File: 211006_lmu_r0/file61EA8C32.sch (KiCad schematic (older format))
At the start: 15 parts

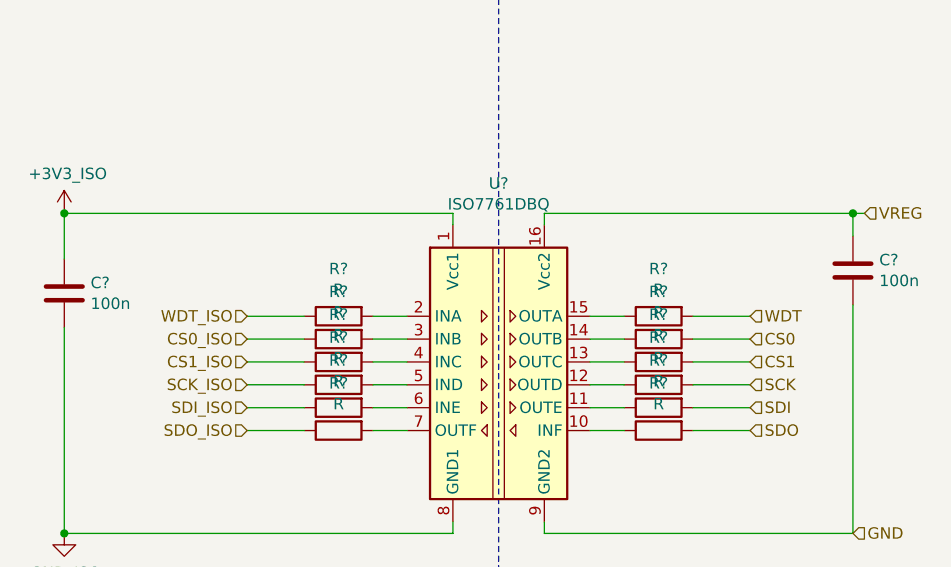
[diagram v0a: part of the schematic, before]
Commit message: Updated BOM and footprints for non-hv components
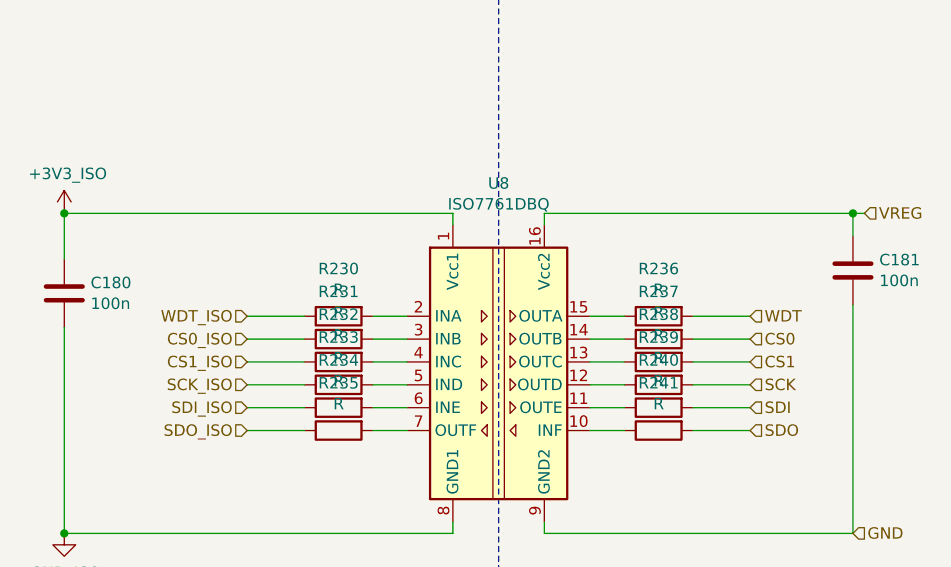
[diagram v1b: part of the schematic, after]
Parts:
- gave numbers to parts that had none: 15
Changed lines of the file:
@@
 SCK_ISO
 $Comp
-L +3v3_iso:+3V3_ISO #PWR?
+L +3v3_iso:+3V3_ISO #PWR0171
 U 1 1 62444AD5
 P 3800 2950
-AR Path="/61EA8C33/62444AD5" Ref="#PWR?"  Part="1"
+AR Path="/61EA8C33/62444AD5" Ref="#PWR0171"  Part="1"
 AR Path="/624497CF/62444AD5" Ref="#PWR?"  Part="1"
 AR Path="/62454BCB/62444AD5" Ref="#PWR?"  Part="1"
-AR Path="/6248C6B3/62444AD5" Ref="#PWR?"  Part="1"
-AR Path="/6248F546/62444AD5" Ref="#PWR?"  Part="1"
-F 0 "#PWR?" H 3800 2800 50  0001 C CNN
+AR Path="/6248C6B3/62444AD5" Ref="#PWR0173"  Part="1"
+AR Path="/6248F546/62444AD5" Ref="#PWR0175"  Part="1"
+F 0 "#PWR0175" H 3800 2800 50  0001 C CNN
 F 1 "+3V3_ISO" H 3815 3123 50  0000 C CNN
 F 2 "" H 3800 2950 50  0001 C CNN
@@
 P 5700 3700
 AR Path="/62454BCB/62479198" Ref="U?"  Part="1"
-AR Path="/61EA8C33/62479198" Ref="U?"  Part="1"
-AR Path="/6248C6B3/62479198" Ref="U?"  Part="1"
-AR Path="/6248F546/62479198" Ref="U?"  Part="1"
-F 0 "U?" H 5700 4581 50  0000 C CNN
+AR Path="/61EA8C33/62479198" Ref="U6"  Part="1"
+AR Path="/6248C6B3/62479198" Ref="U7"  Part="1"
+AR Path="/6248F546/62479198" Ref="U8"  Part="1"
+F 0 "U8" H 5700 4581 50  0000 C CNN
 F 1 "ISO7761DBQ" H 5700 4490 50  0000 C CNN
 F 2 "Package_SO:SSOP-16_3.9x4.9mm_P0.635mm" H 5925 3150 50  0001 L CNN
@@
 P 7250 3200
 AR Path="/62454BCB/6247B7F3" Ref="C?"  Part="1"
-AR Path="/61EA8C33/6247B7F3" Ref="C?"  Part="1"
-AR Path="/6248C6B3/6247B7F3" Ref="C?"  Part="1"
-AR Path="/6248F546/6247B7F3" Ref="C?"  Part="1"
-F 0 "C?" H 7365 3246 50  0000 L CNN
+AR Path="/61EA8C33/6247B7F3" Ref="C177"  Part="1"
+AR Path="/6248C6B3/6247B7F3" Ref="C179"  Part="1"
+AR Path="/6248F546/6247B7F3" Ref="C181"  Part="1"
+F 0 "C181" H 7365 3246 50  0000 L CNN
 F 1 "100n" H 7365 3155 50  0000 L CNN
 F 2 "" H 7288 3050 50  0001 C CNN
@@
 P 3800 3300
 AR Path="/62454BCB/6247C6BA" Ref="C?"  Part="1"
-AR Path="/61EA8C33/6247C6BA" Ref="C?"  Part="1"
-AR Path="/6248C6B3/6247C6BA" Ref="C?"  Part="1"
-AR Path="/6248F546/6247C6BA" Ref="C?"  Part="1"
-F 0 "C?" H 3915 3346 50  0000 L CNN
+AR Path="/61EA8C33/6247C6BA" Ref="C176"  Part="1"
+AR Path="/6248C6B3/6247C6BA" Ref="C178"  Part="1"
+AR Path="/6248F546/6247C6BA" Ref="C180"  Part="1"
+F 0 "C180" H 3915 3346 50  0000 L CNN
 F 1 "100n" H 3915 3255 50  0000 L CNN
 F 2 "" H 3838 3150 50  0001 C CNN
@@
 $EndComp
 $Comp
-L gnd_iso:GND_ISO #PWR?
+L gnd_iso:GND_ISO #PWR0172
 U 1 1 62445214
 P 3800 4350
-AR Path="/61EA8C33/62445214" Ref="#PWR?"  Part="1"
+AR Path="/61EA8C33/62445214" Ref="#PWR0172"  Part="1"
 AR Path="/624497CF/62445214" Ref="#PWR?"  Part="1"
 AR Path="/62454BCB/62445214" Ref="#PWR?"  Part="1"
-AR Path="/6248C6B3/62445214" Ref="#PWR?"  Part="1"
-AR Path="/6248F546/62445214" Ref="#PWR?"  Part="1"
-F 0 "#PWR?" H 3800 4100 50  0001 C CNN
+AR Path="/6248C6B3/62445214" Ref="#PWR0174"  Part="1"
+AR Path="/6248F546/62445214" Ref="#PWR0176"  Part="1"
+F 0 "#PWR0176" H 3800 4100 50  0001 C CNN
 F 1 "GND_ISO" H 3805 4177 50  0000 C CNN
 F 2 "" H 3800 4350 50  0001 C CNN
@@
 	5500 2950 5500 3000
 $Comp
-L Device:R R?
+L Device:R R206
 U 1 1 626BF8F2
 P 5000 3400
-F 0 "R?" V 4793 3400 50  0000 C CNN
+AR Path="/61EA8C33/626BF8F2" Ref="R206"  Part="1"
+AR Path="/6248C6B3/626BF8F2" Ref="R218"  Part="1"
+AR Path="/6248F546/626BF8F2" Ref="R230"  Part="1"
+F 0 "R230" V 4793 3400 50  0000 C CNN
 F 1 "R" V 4884 3400 50  0000 C CNN
 F 2 "" V 4930 3400 50  0001 C CNN
@@
 $EndComp
 $Comp
-L Device:R R?
+L Device:R R207
 U 1 1 626C0FC4
 P 5000 3500
-F 0 "R?" V 4793 3500 50  0000 C CNN
+AR Path="/61EA8C33/626C0FC4" Ref="R207"  Part="1"
+AR Path="/6248C6B3/626C0FC4" Ref="R219"  Part="1"
+AR Path="/6248F546/626C0FC4" Ref="R231"  Part="1"
+F 0 "R231" V 4793 3500 50  0000 C CNN
 F 1 "R" V 4884 3500 50  0000 C CNN
 F 2 "" V 4930 3500 50  0001 C CNN
@@
 $EndComp
 $Comp
-L Device:R R?
+L Device:R R208
 U 1 1 626C1186
 P 5000 3600
-F 0 "R?" V 4793 3600 50  0000 C CNN
+AR Path="/61EA8C33/626C1186" Ref="R208"  Part="1"
+AR Path="/6248C6B3/626C1186" Ref="R220"  Part="1"
+AR Path="/6248F546/626C1186" Ref="R232"  Part="1"
+F 0 "R232" V 4793 3600 50  0000 C CNN
 F 1 "R" V 4884 3600 50  0000 C CNN
 F 2 "" V 4930 3600 50  0001 C CNN
@@
 $EndComp
 $Comp
-L Device:R R?
+L Device:R R209
 U 1 1 626C1339
 P 5000 3700
-F 0 "R?" V 4793 3700 50  0000 C CNN
+AR Path="/61EA8C33/626C1339" Ref="R209"  Part="1"
+AR Path="/6248C6B3/626C1339" Ref="R221"  Part="1"
+AR Path="/6248F546/626C1339" Ref="R233"  Part="1"
+F 0 "R233" V 4793 3700 50  0000 C CNN
 F 1 "R" V 4884 3700 50  0000 C CNN
 F 2 "" V 4930 3700 50  0001 C CNN
@@
 $EndComp
 $Comp
-L Device:R R?
+L Device:R R210
 U 1 1 626C148E
 P 5000 3800
-F 0 "R?" V 4793 3800 50  0000 C CNN
+AR Path="/61EA8C33/626C148E" Ref="R210"  Part="1"
+AR Path="/6248C6B3/626C148E" Ref="R222"  Part="1"
+AR Path="/6248F546/626C148E" Ref="R234"  Part="1"
+F 0 "R234" V 4793 3800 50  0000 C CNN
 F 1 "R" V 4884 3800 50  0000 C CNN
 F 2 "" V 4930 3800 50  0001 C CNN
@@
 $EndComp
 $Comp
-L Device:R R?
+L Device:R R211
 U 1 1 626C1651
 P 5000 3900
-F 0 "R?" V 4793 3900 50  0000 C CNN
+AR Path="/61EA8C33/626C1651" Ref="R211"  Part="1"
+AR Path="/6248C6B3/626C1651" Ref="R223"  Part="1"
+AR Path="/6248F546/626C1651" Ref="R235"  Part="1"
+F 0 "R235" V 4793 3900 50  0000 C CNN
 F 1 "R" V 4884 3900 50  0000 C CNN
 F 2 "" V 4930 3900 50  0001 C CNN
@@
 $EndComp
 $Comp
-L Device:R R?
+L Device:R R212
 U 1 1 626C3188
 P 6400 3400
-F 0 "R?" V 6193 3400 50  0000 C CNN
+AR Path="/61EA8C33/626C3188" Ref="R212"  Part="1"
+AR Path="/6248C6B3/626C3188" Ref="R224"  Part="1"
+AR Path="/6248F546/626C3188" Ref="R236"  Part="1"
+F 0 "R236" V 6193 3400 50  0000 C CNN
 F 1 "R" V 6284 3400 50  0000 C CNN
 F 2 "" V 6330 3400 50  0001 C CNN
@@
 $EndComp
 $Comp
-L Device:R R?
+L Device:R R213
 U 1 1 626C318E
 P 6400 3500
-F 0 "R?" V 6193 3500 50  0000 C CNN
+AR Path="/61EA8C33/626C318E" Ref="R213"  Part="1"
+AR Path="/6248C6B3/626C318E" Ref="R225"  Part="1"
+AR Path="/6248F546/626C318E" Ref="R237"  Part="1"
+F 0 "R237" V 6193 3500 50  0000 C CNN
 F 1 "R" V 6284 3500 50  0000 C CNN
 F 2 "" V 6330 3500 50  0001 C CNN
@@
 $EndComp
 $Comp
-L Device:R R?
+L Device:R R214
 U 1 1 626C3194
 P 6400 3600
-F 0 "R?" V 6193 3600 50  0000 C CNN
+AR Path="/61EA8C33/626C3194" Ref="R214"  Part="1"
+AR Path="/6248C6B3/626C3194" Ref="R226"  Part="1"
+AR Path="/6248F546/626C3194" Ref="R238"  Part="1"
+F 0 "R238" V 6193 3600 50  0000 C CNN
 F 1 "R" V 6284 3600 50  0000 C CNN
 F 2 "" V 6330 3600 50  0001 C CNN
@@
 $EndComp
 $Comp
-L Device:R R?
+L Device:R R215
 U 1 1 626C319A
 P 6400 3700
-F 0 "R?" V 6193 3700 50  0000 C CNN
+AR Path="/61EA8C33/626C319A" Ref="R215"  Part="1"
+AR Path="/6248C6B3/626C319A" Ref="R227"  Part="1"
+AR Path="/6248F546/626C319A" Ref="R239"  Part="1"
+F 0 "R239" V 6193 3700 50  0000 C CNN
 F 1 "R" V 6284 3700 50  0000 C CNN
 F 2 "" V 6330 3700 50  0001 C CNN
@@
 $EndComp
 $Comp
-L Device:R R?
+L Device:R R216
 U 1 1 626C31A0
 P 6400 3800
-F 0 "R?" V 6193 3800 50  0000 C CNN
+AR Path="/61EA8C33/626C31A0" Ref="R216"  Part="1"
+AR Path="/6248C6B3/626C31A0" Ref="R228"  Part="1"
+AR Path="/6248F546/626C31A0" Ref="R240"  Part="1"
+F 0 "R240" V 6193 3800 50  0000 C CNN
 F 1 "R" V 6284 3800 50  0000 C CNN
 F 2 "" V 6330 3800 50  0001 C CNN
@@
 $EndComp
 $Comp
-L Device:R R?
+L Device:R R217
 U 1 1 626C31A6
 P 6400 3900
-F 0 "R?" V 6193 3900 50  0000 C CNN
+AR Path="/61EA8C33/626C31A6" Ref="R217"  Part="1"
+AR Path="/6248C6B3/626C31A6" Ref="R229"  Part="1"
+AR Path="/6248F546/626C31A6" Ref="R241"  Part="1"
+F 0 "R241" V 6193 3900 50  0000 C CNN
 F 1 "R" V 6284 3900 50  0000 C CNN
 F 2 "" V 6330 3900 50  0001 C CNN

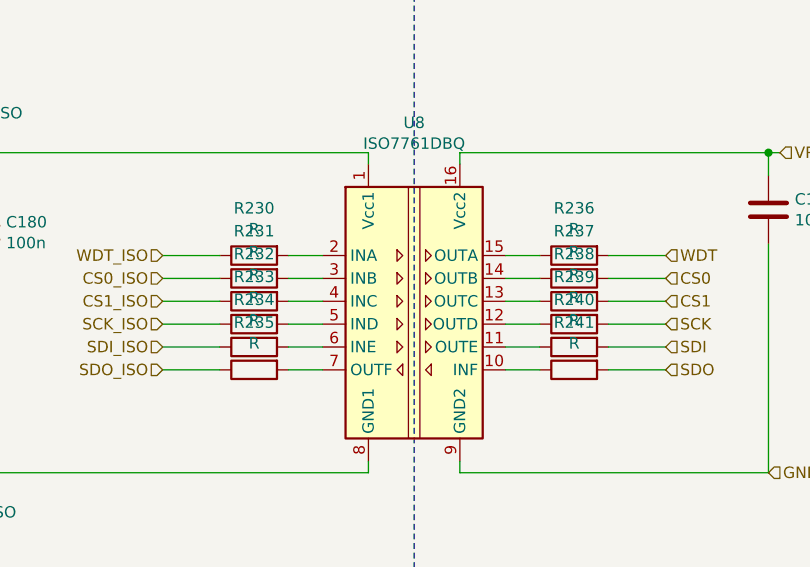
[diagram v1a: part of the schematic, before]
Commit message: Added most footprint requirements in HV
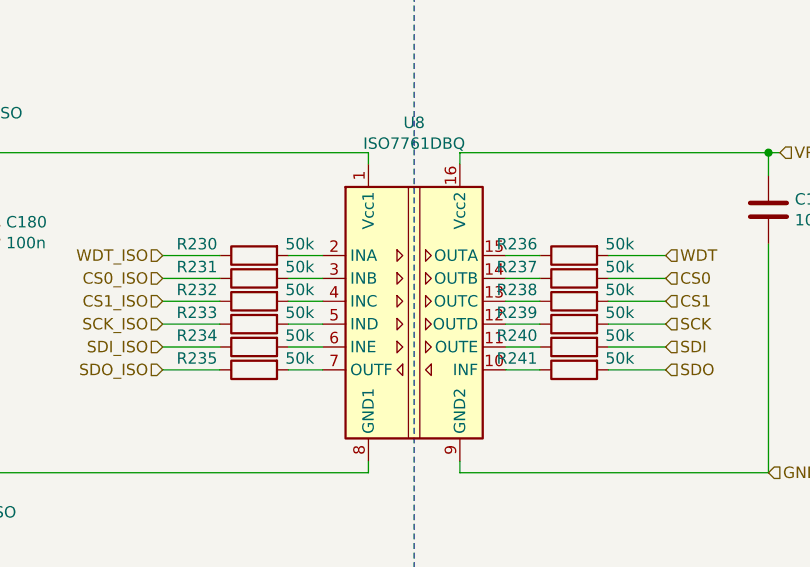
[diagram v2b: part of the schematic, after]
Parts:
- C176, C177: footprint (none) -> Capacitor_SMD:C_0603_1608Metric_Pad1.08x0.95mm_HandSolder
- R206, R207, R208, R209, R210, R211, R212, R213, R214, R215, R216, R217: value R -> 50k; footprint (none) -> Resistor_SMD:R_0603_1608Metric_Pad0.98x0.95mm_HandSolder

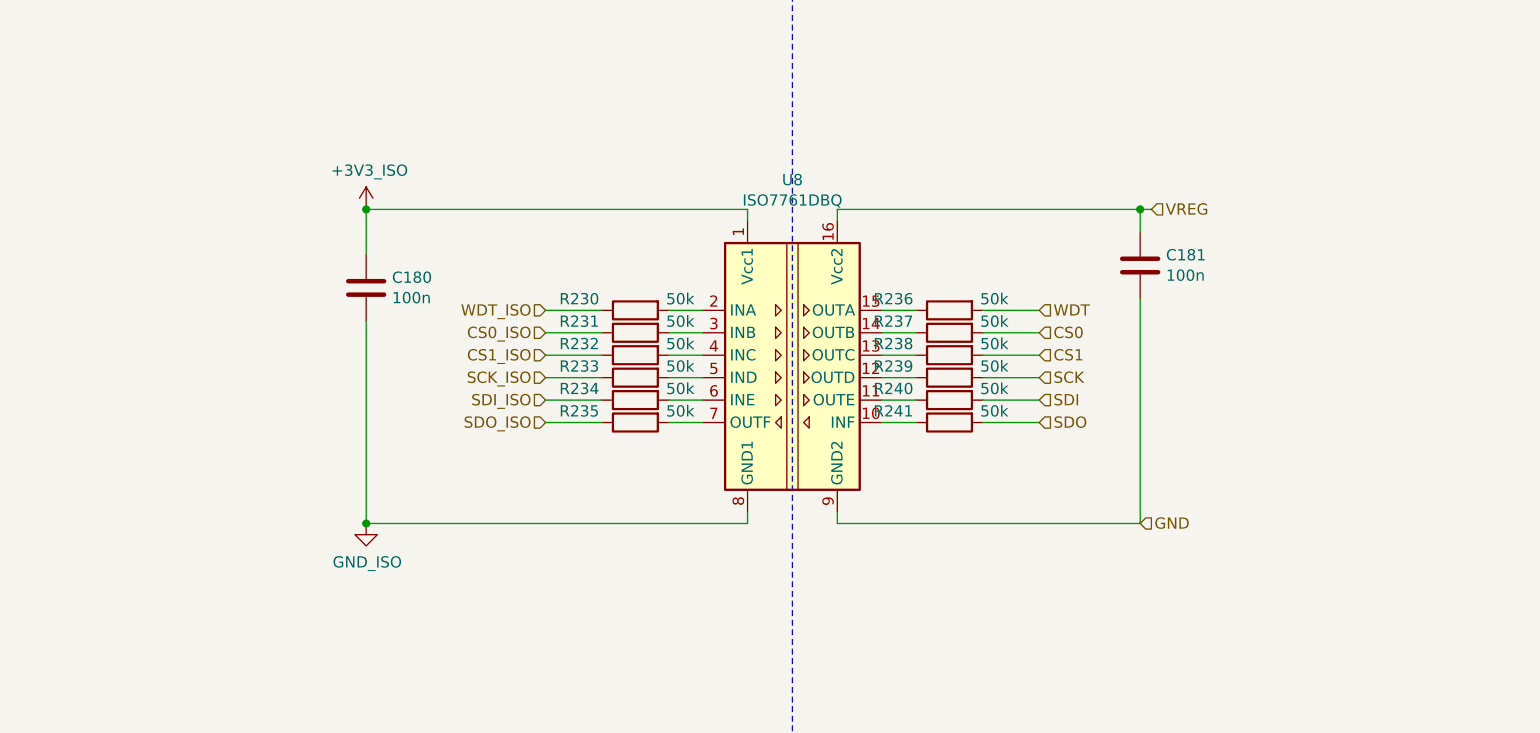
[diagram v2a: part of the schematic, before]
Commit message: Updated with Mouser links for BOM
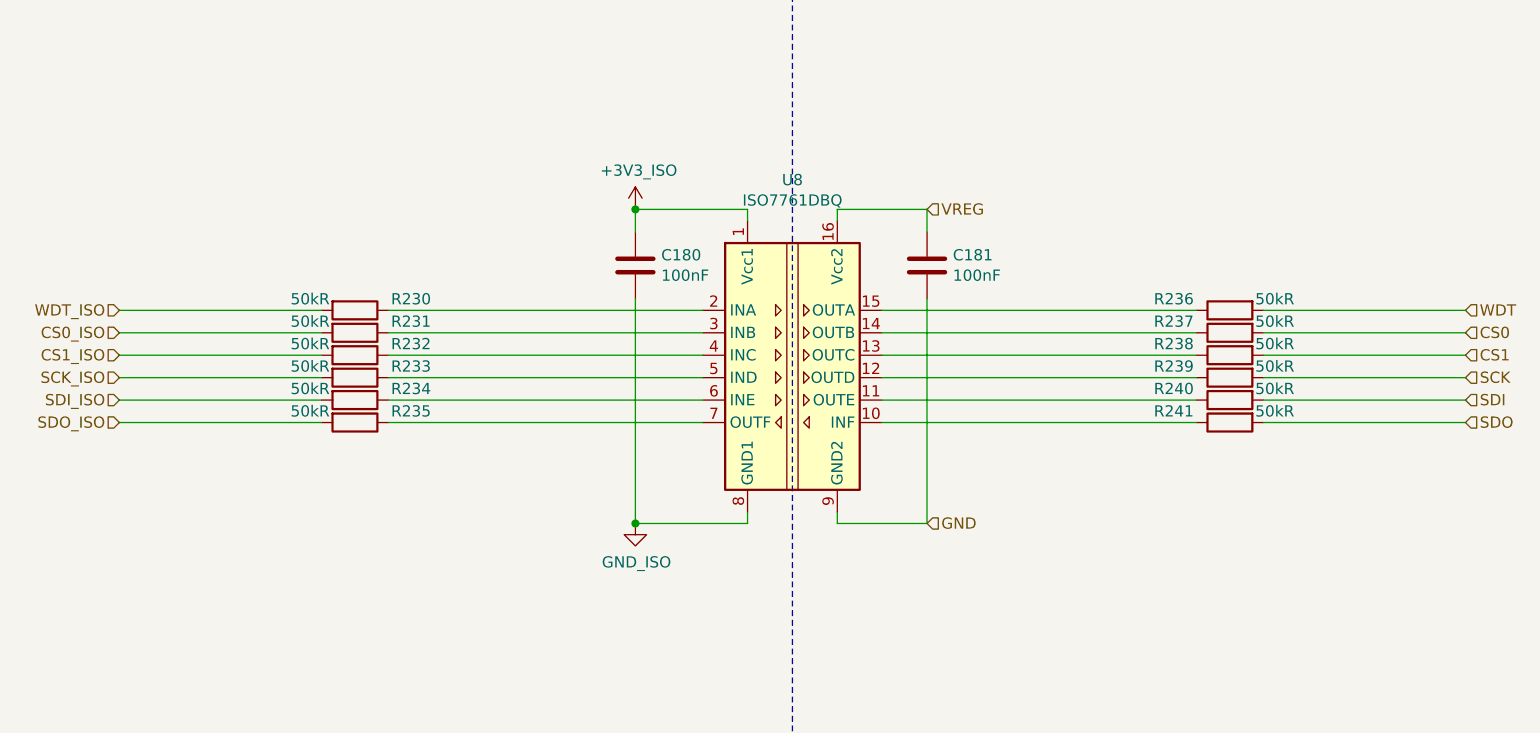
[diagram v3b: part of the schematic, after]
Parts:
- C176, C177: value 100n -> 100nF
- R206, R207, R208, R209, R210, R211, R212, R213, R214, R215, R216, R217: value 50k -> 50kR
- U6: Manufacturer (none) -> Texas Instruments; Mouser Part Number (none) -> NOT AVAILABLE!; Mouser URL (none) -> NOT AVAILABLE!; Part Number (none) -> ISO7761DBQ
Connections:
- net CS0_ISO: now also R207.2; no longer R207.1
- net CS1_ISO: now also R208.2; no longer R208.1
- net SCK_ISO: now also R209.2; no longer R209.1
- net SDI_ISO: now also R210.2; no longer R210.1
- net SDO_ISO: now also R211.2; no longer R211.1
- net WDT_ISO: now also R206.2; no longer R206.1
- net at U6.3 (INB): now also R207.1; no longer R207.2
- net at U6.4 (INC): now also R208.1; no longer R208.2
- net at U6.5 (IND): now also R209.1; no longer R209.2
- net at U6.6 (INE): now also R210.1; no longer R210.2
- net at U6.7 (OUTF): now also R211.1; no longer R211.2
- net at U6.2 (INA): now also R206.1; no longer R206.2
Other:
- moved on the sheet: C180, C181, R236, R237, R238, R239, R240, R241
